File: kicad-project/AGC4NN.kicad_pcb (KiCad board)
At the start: 2 copper layers, 18 x 12 mm, 13 parts, among them J1 Conn_01x04, Q1 MMBT3904, Q2 2N7002

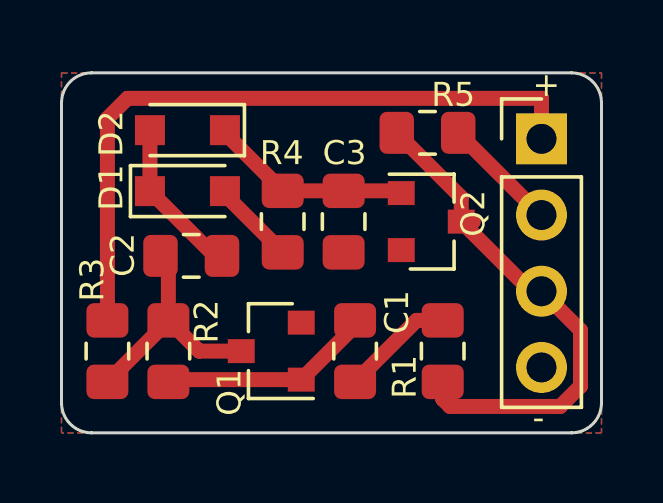
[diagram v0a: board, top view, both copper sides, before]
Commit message: Add XI logo to PCB.
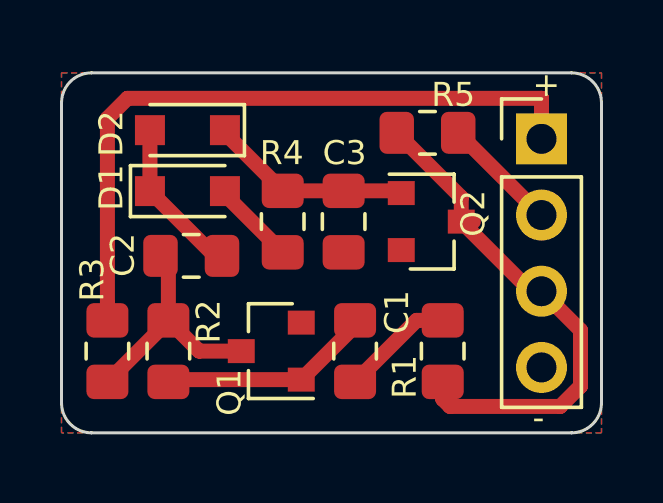
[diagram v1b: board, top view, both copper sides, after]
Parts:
- added G***: LOGO, xi:xi-logo-a-07_07, B.Cu at (61.5, 46.0)
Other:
- board text added: "AGC4NN v01.c BG1REN 20200104"
- board text added: "JLCJLCJLCJLC"
- board text removed: "BG1REN 20200101 AGC4NN v01.c, CQ11"
